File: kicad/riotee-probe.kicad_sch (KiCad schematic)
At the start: 0 parts

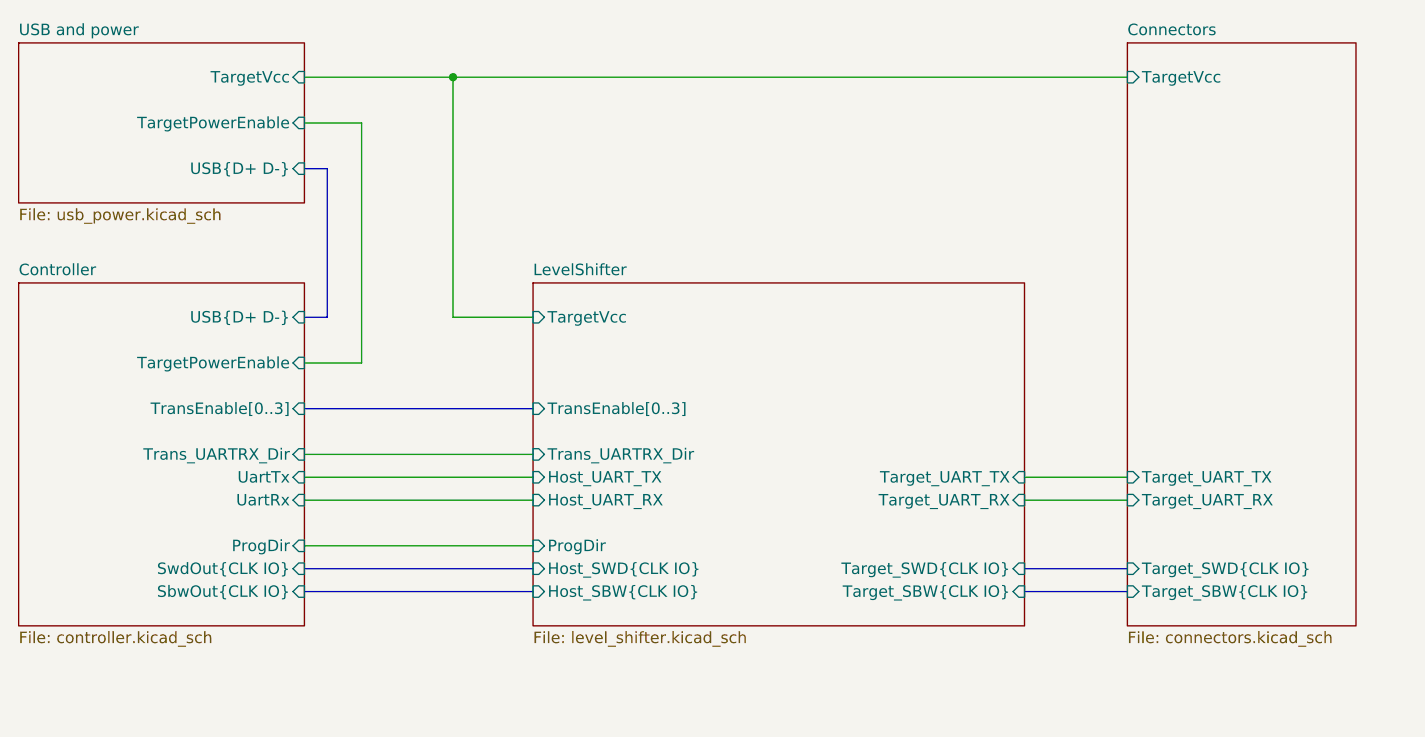
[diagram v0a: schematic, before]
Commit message: add fourth level converter for simultaneous programming + TX/RX
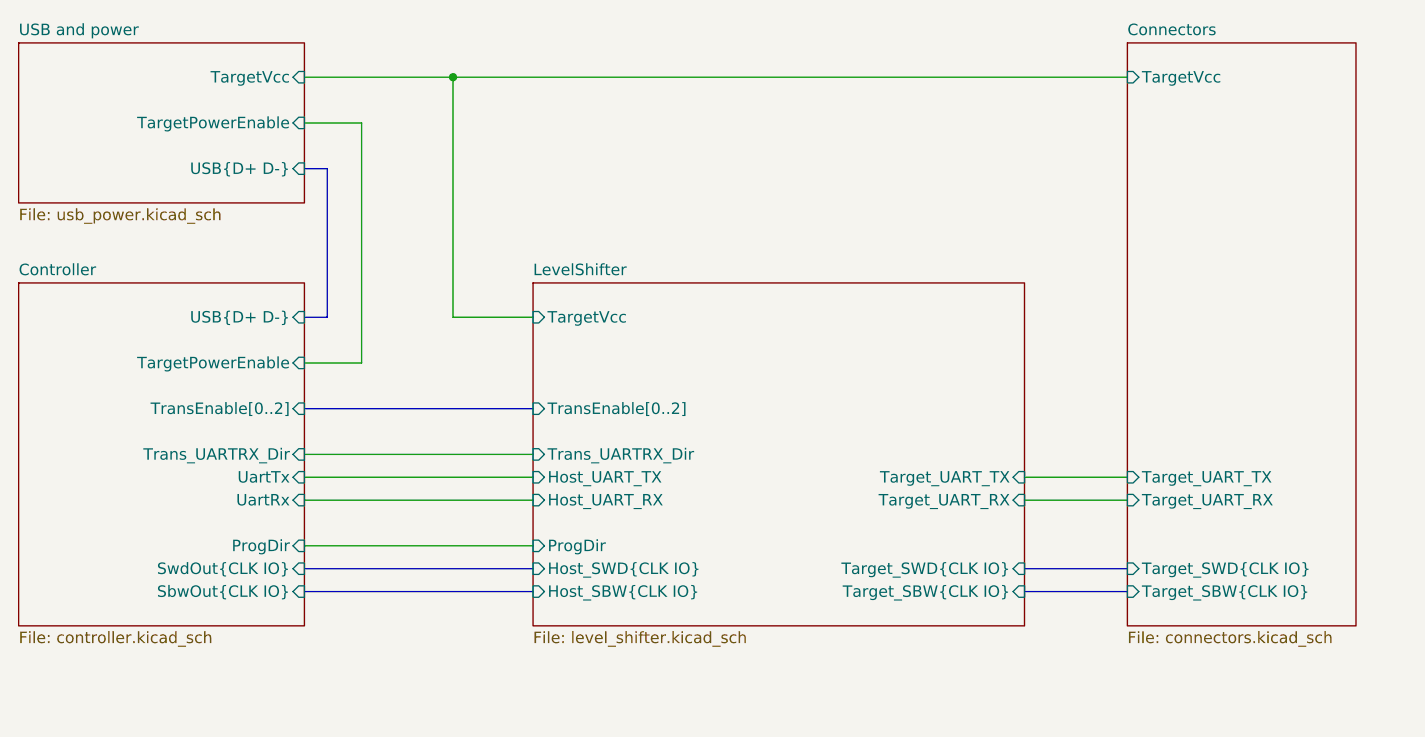
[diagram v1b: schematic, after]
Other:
- sheet Controller ports: added TransEnable[0..2]; removed TransEnable[0..3]
- sheet LevelShifter ports: added TransEnable[0..2]; removed TransEnable[0..3]

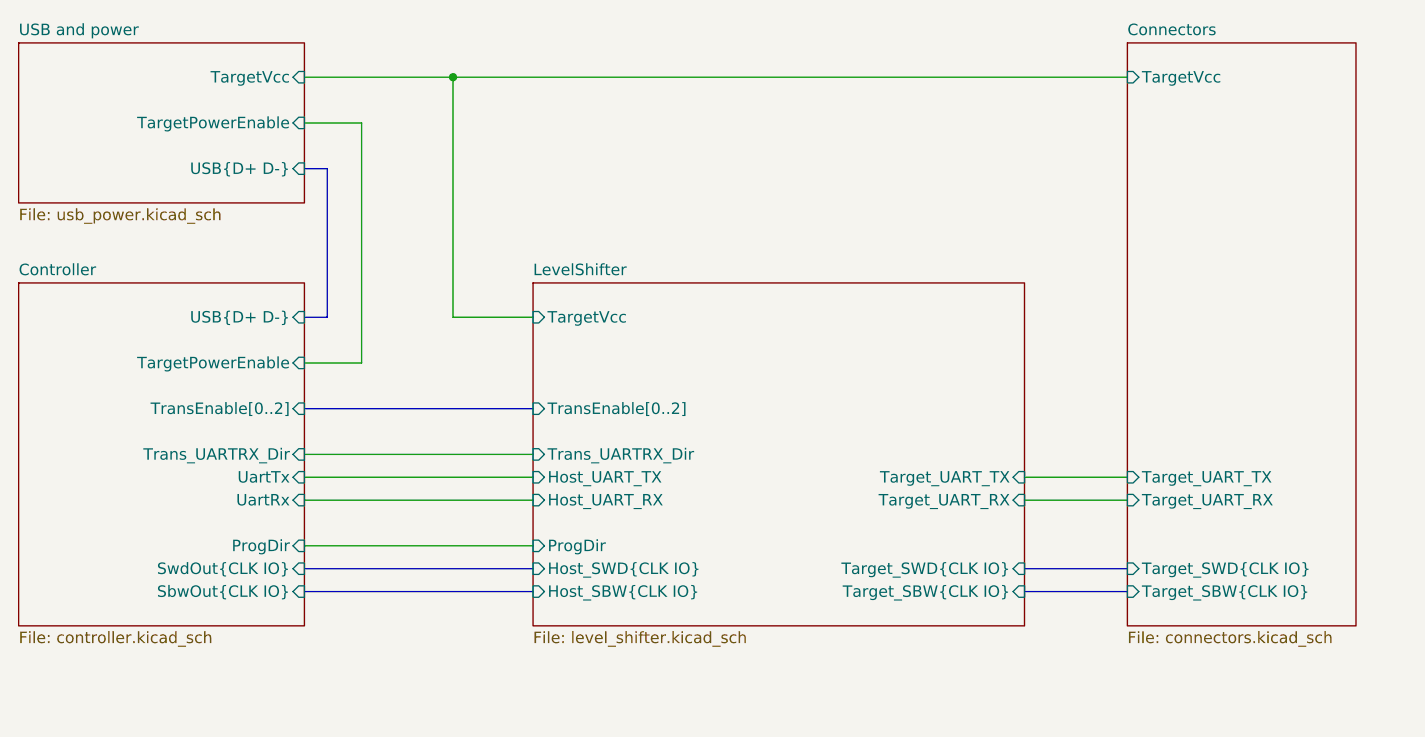
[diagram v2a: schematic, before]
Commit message: replace target supply diode with analog switch
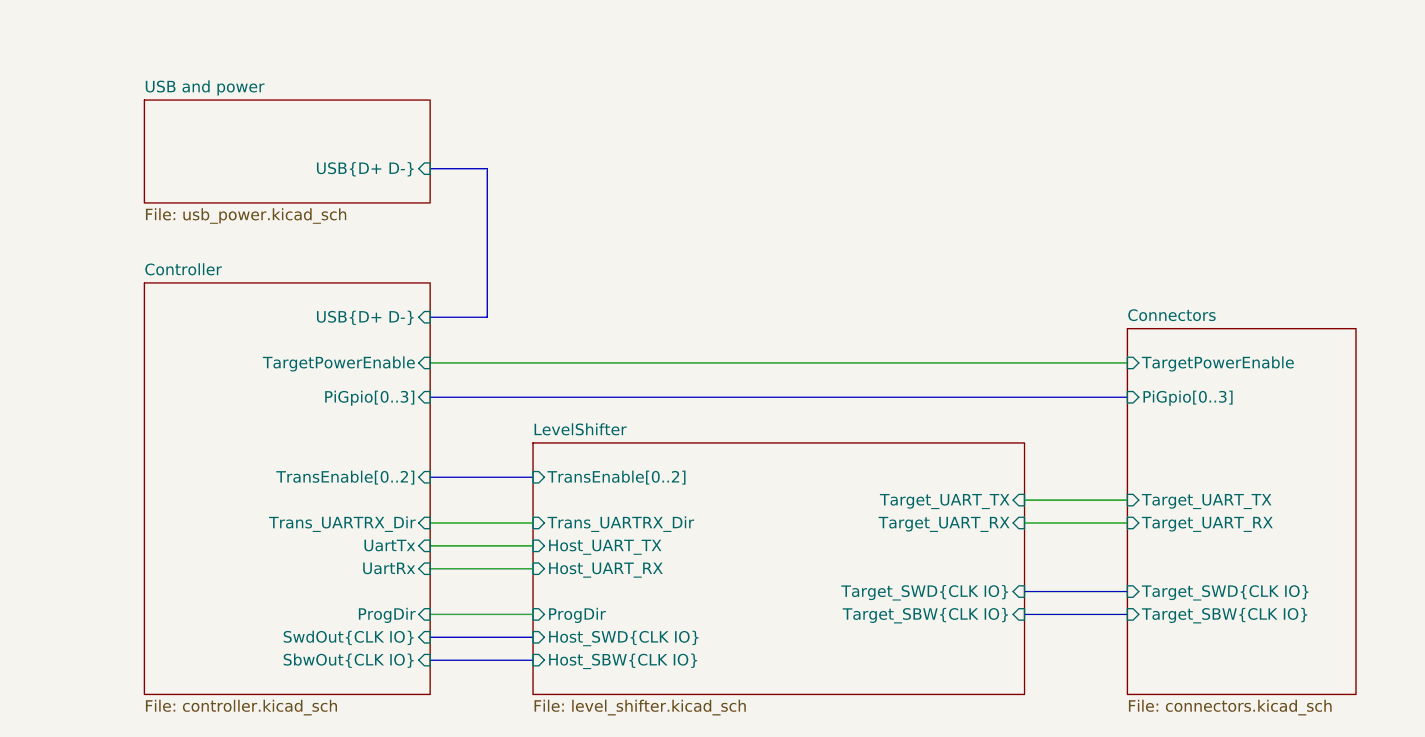
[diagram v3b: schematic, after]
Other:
- sheet Connectors ports: added PiGpio[0..3], TargetPowerEnable; removed TargetVcc
- sheet Controller ports: added PiGpio[0..3]; removed none
- sheet LevelShifter ports: added none; removed TargetVcc
- sheet USB and power ports: added none; removed TargetPowerEnable, TargetVcc
